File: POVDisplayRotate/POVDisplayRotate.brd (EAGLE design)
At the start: 54 x 82 mm, 38 parts, among them U1 CY8CKIT-142, U2 STP08DP05, U3 STP08DP05, U4 STP08DP05, U5 MPQ4420Q

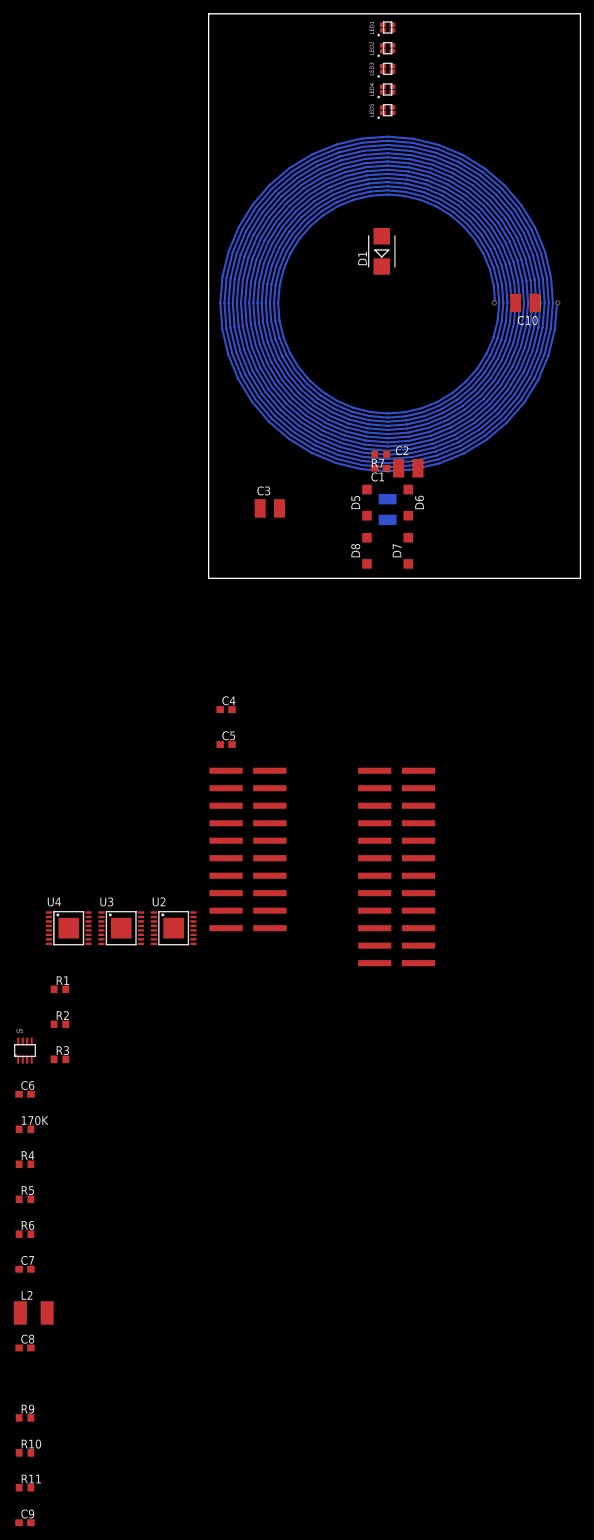
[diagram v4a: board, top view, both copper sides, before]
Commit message: Placed most of the components for the POVRotate. Working on PCB.
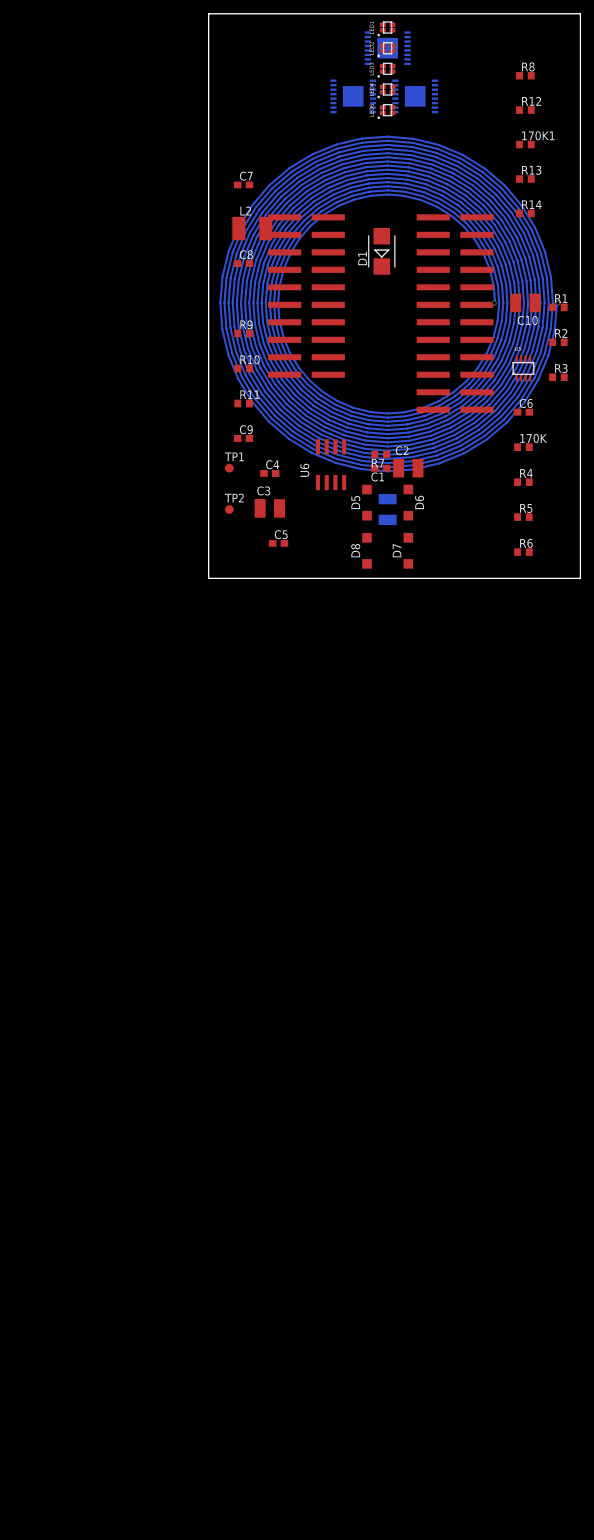
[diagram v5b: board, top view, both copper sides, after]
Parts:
- added 170K1: 120, resistor:R0603
- added R12: 820k, resistor:R0603
- added R13: 12k, resistor:R0603
- added R14: 3k, resistor:R0603
- added R8: 33k, resistor:R0603
- added TP1, TP2: TPB1,27, testpad:B1,27
- added U6: M95M01, NicksParts:SO-08
- moved C8 160.6 mm to (5.08, 45.7)
- moved L2 160.6 mm to (6.35, 50.8)
- moved R11 160.6 mm to (5.08, 25.4)
- moved R9 160.6 mm to (5.08, 35.6)
- moved C7 160.6 mm to (5.08, 57.1)
- moved C9 160.6 mm to (5.08, 20.3)
- moved R10 160.6 mm to (5.08, 30.5)
- moved U2 131.5 mm to (26.0, 77.0), flipped to the bottom, turned to 180 degrees
- moved U3 128.1 mm to (30.0, 70.0), flipped to the bottom
- moved U4 127.7 mm to (21.0, 70.0), flipped to the bottom
- moved 170K 122.7 mm to (45.7, 19.1)
- moved C6 122.7 mm to (45.7, 24.1)
- moved R1 122.7 mm to (50.8, 39.4)
- moved R2 122.7 mm to (50.8, 34.3)
- moved R3 122.7 mm to (50.8, 29.2)
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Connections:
- new net DAC_OUT: R13.2, R14.1, U1.2.1
- new net EE_CS: U1.0.2, U6.1
- new net EE_HOLD: U6.7
- new net EE_MISO: U1.0.1, U6.2
- new net EE_MOSI: U1.0.0, U6.5
- new net EE_SCLK: U1.0.3, U6.6
- new net EE_WP: U6.3
- new net GND: U6.4
- new net IN_PWR: R12.2, R8.1, U1.3.0
- new net N$13: TP1.TP, U5.1
- new net N$16: 170K1.1, C2.1, D5.C, D8.C
- new net N$3: U1.1.6
- net AGND: now also R14.2, R8.2
- net OPAMP1_NEG: now also U1.2.4, U1.2.7
- net OPAMP1_OUT: now also TP2.TP, U1.2.3
- net SCLK: now also U1.1.7
- net SDI: now also U1.0.4
- net V+: now also 170K1.2, R12.1; no longer C2.1, D5.C, D8.C
- net VCC: now also R13.1, U6.8

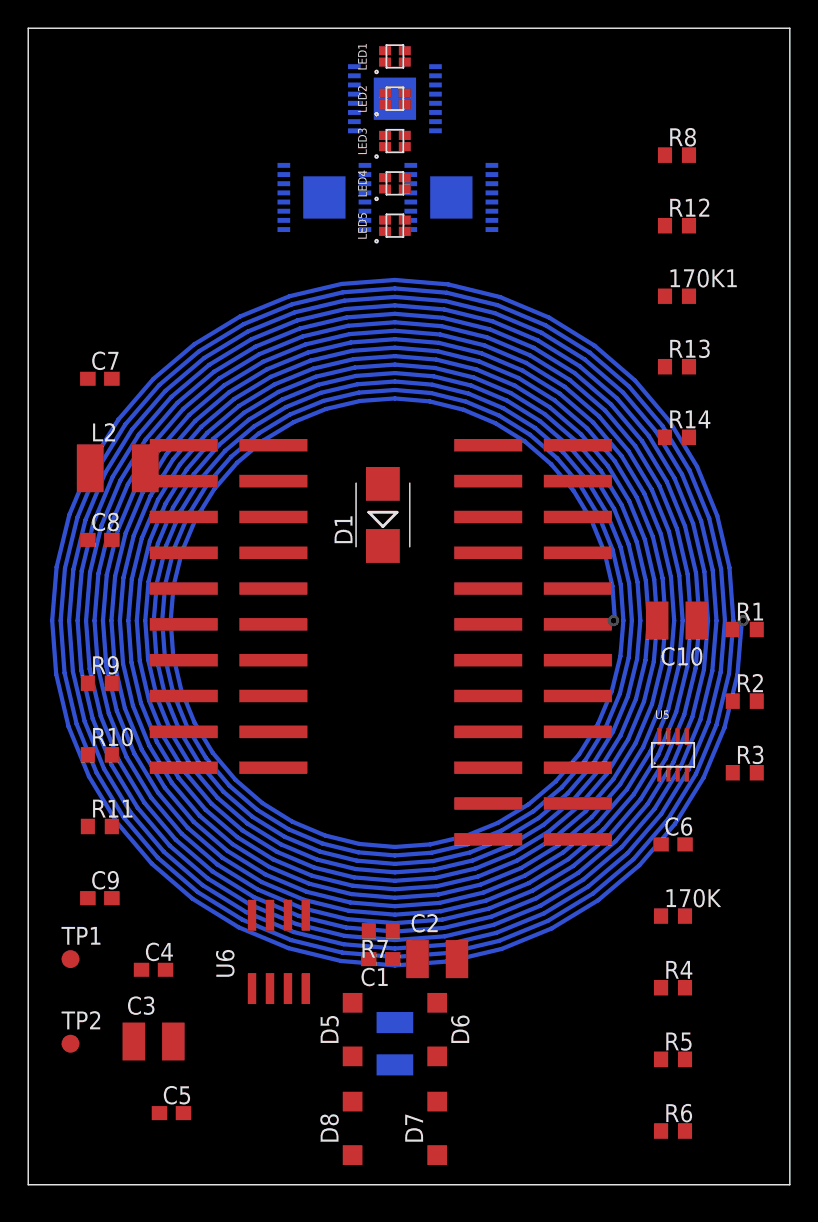
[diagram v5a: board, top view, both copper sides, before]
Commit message: Working on the routing of the POVRotate display.
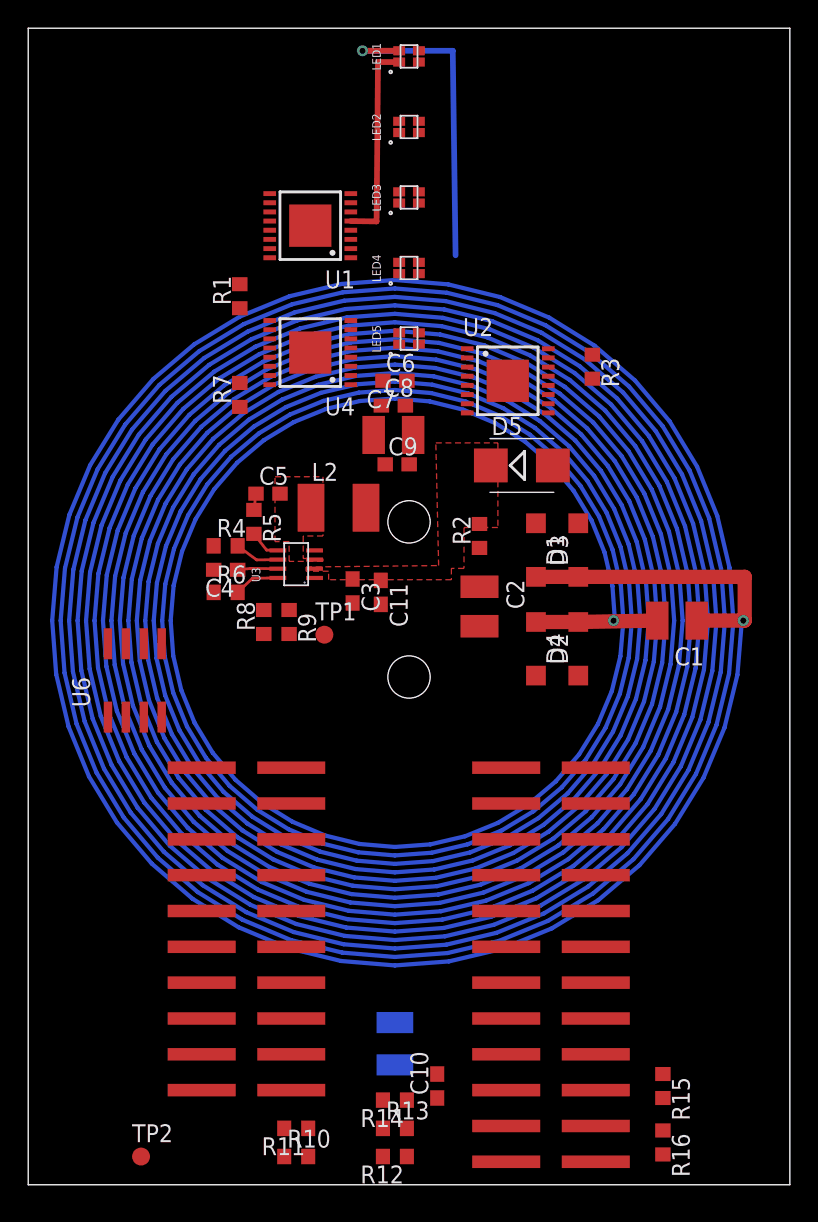
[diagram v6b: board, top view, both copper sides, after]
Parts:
- removed 170K, 170K1: 120, resistor:R0603
- removed D7, D8: (no value), diode:SOD123
- added C11: 0.1u, resistor:C0603
- added D3, D4: (no value), diode:SOD123
- added R15: 12k, resistor:R0603
- added R16: 3k, resistor:R0603
- C1: value 22u -> 100n; device resistor:C0603 -> resistor:C1210
- C10: value 100n -> 5p; device resistor:C1210 -> resistor:C0603
- C3: value 100u -> 22u; device resistor:C1210 -> resistor:C0603
- C4: value 10u -> 0.1u
- C5: value 1u -> 100n
- C6: value 0.1u -> 47u
- C7: value 100n -> 100u; device resistor:C0603 -> resistor:C1210
- C8: value 47u -> 10u
- C9: value 5p -> 1u
- D1: device diode:SMB -> diode:SOD123
- D2: value OP980 -> (none); device NicksParts:PLCC-2 -> diode:SOD123
- D5: device diode:SOD123 -> diode:SMB
- D6: value (none) -> OP980; device diode:SOD123 -> NicksParts:PLCC-2
- R13: value 12k -> 33k
- R14: value 3k -> 100k
- R2: value 386 -> 120
- R4: value 41.2k -> 120
- R5: value 12k -> 20
- R6: value 20 -> 51k
- R7: value 51k -> 386
- R8: value 33k -> 12k
- R9: value 100k -> 41.2k
- U1: value CY8CKIT-142 -> STP08DP05; device NicksParts:CY8CKIT-142 -> NicksParts:SSOP16_EPAD
- U3: value STP08DP05 -> MPQ4420Q; device NicksParts:SSOP16_EPAD -> NicksParts:SOT-23-8
- U5: value MPQ4420Q -> CY8CKIT-142; device NicksParts:SOT-23-8 -> NicksParts:CY8CKIT-142
- moved R12 69.0 mm to (26.0, 2.00), turned to 180 degrees
- moved R13 57.6 mm to (26.0, 4.00)
- moved R14 51.1 mm to (26.0, 6.00), turned to 180 degrees
- moved R6 49.6 mm to (14.0, 42.0)
- moved R5 48.3 mm to (16.0, 47.0), turned to 270 degrees
- moved R4 44.6 mm to (14.0, 45.3)
- moved C5 44.4 mm to (17.0, 49.0)
- moved R8 44.2 mm to (16.7, 39.9), turned to 90 degrees
- moved R1 42.9 mm to (15.0, 63.0), turned to 90 degrees
- moved D5 41.8 mm to (35.0, 51.0), turned to 0 degrees
- moved R7 39.3 mm to (15.0, 56.0), turned to 90 degrees
- moved C6 38.3 mm to (26.0, 57.0)
- moved C9 37.3 mm to (26.2, 51.1)
- moved C10 37.1 mm to (29.0, 7.00), turned to 90 degrees
- moved C3 34.9 mm to (23.0, 42.1), turned to 270 degrees
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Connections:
- removed net N$9: C7.2, L2.1, U5.3
- new net SWOUT: C5.2, L2.1, U3.3
- net AGND: now also C11.2, C7.2, C9.2, D2.A, D5.A, D6.P$1, R13.2, R16.2, R7.2, U1.1, U3.4, U5.GND, U5.GND1, U5.GND2; no longer C1.2, C5.2, D2.P$1, D6.A, D7.A, R14.2, R2.2, R5.2, U1.GND1, U1.GND2, U3.1, U3.GND, U5.4
- net DAC_OUT: now also R15.2, R16.1, U5.2.1; no longer R13.2, R14.1, U1.2.1
- net EE_CS: now also U5.0.2; no longer U1.0.2
- net EE_MISO: now also U5.0.1; no longer U1.0.1
- net EE_MOSI: now also U5.0.0; no longer U1.0.0
- net EE_SCLK: now also U5.0.3; no longer U1.0.3
- net GLED1: now also U2.5; no longer U3.5
- net GLED2: now also U2.6; no longer U3.6
- net GLED3: now also U2.7; no longer U3.7
- net GLED4: now also U2.8; no longer U3.8
- net GLED5: now also U2.9; no longer U3.9
- net IN_PWR: now also R13.1, U5.3.0; no longer R8.1, U1.3.0
- net LE1: now also U1.4; no longer U2.4
- net LE2: now also U2.4; no longer U3.4
- net N$1: now also C4.1, U3.7; no longer C6.1, U5.7
- net N$10: now also R3.1, U2.15; no longer R2.1, U3.15
- net N$11: now also U2.14; no longer U3.14
- net N$12: now also R7.1; no longer R3.1
- net N$13: now also U3.1; no longer U5.1
- net N$16: now also D3.C, D4.C, R2.1; no longer 170K1.1, D5.C, D8.C
- net N$18: now also U1.14, U2.2; no longer U2.14, U3.2
- net N$2: now also R4.2, U3.6; no longer 170K.2, U5.6
- net N$3: now also U5.1.6; no longer U1.1.6
- net N$4: now also R6.2, U3.8; no longer R7.2, U5.8
- net N$5: now also R6.1, R8.1, R9.2; no longer R4.2, R5.1, R7.1
- net N$6: now also U1.15; no longer U2.15
- net N$7: now also R5.2, U3.5; no longer R6.2, U5.5
- net N$8: now also C5.1, R5.1; no longer C7.1, R6.1
- net NEG_COIL: now also C1.2, D2.C, D4.A; no longer C10.2, D7.C, D8.A
- net OE1: now also U1.13; no longer U2.13
- net OE2: now also U2.13; no longer U3.13
- net OPAMP1_NEG: now also C10.2, D6.P$2, R14.2, U5.2.4, U5.2.7; no longer C9.2, D2.P$2, R9.2, U1.2.4, U1.2.7
- net OPAMP1_OUT: now also C10.1, R14.1, U5.2.3; no longer C9.1, R9.1, U1.2.3
- net POS_COIL: now also C1.1, D1.C, D3.A; no longer C10.1, D5.A, D6.C
- net RLED1: now also U1.5; no longer U2.5
- net RLED2: now also U1.6; no longer U2.6
- net RLED3: now also U1.7; no longer U2.7
- net RLED4: now also U1.8; no longer U2.8
- net RLED5: now also U1.9; no longer U2.9
- net SCLK: now also U1.3, U5.1.7; no longer U1.1.7, U3.3
- net SDI: now also U1.2, U5.0.4; no longer U1.0.4, U2.2
- net V+: now also C11.1, C3.1, D5.C, R2.2, R4.1, U3.2; no longer 170K.1, 170K1.2, C1.1, D1.C, U5.2
- net VCC: now also C6.1, C7.1, C9.1, R15.1, R9.1, U1.16, U5.VDDA, U5.VDDD, U5.VDDR; no longer C3.1, C4.1, C5.1, R13.1, R4.1, U1.VDDA, U1.VDDD, U1.VDDR, U3.16
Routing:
- net GLED1: track 0.00 -> 23.5 mm, vias 0 -> 1
- net POS_COIL: track 0.00 -> 21.3 mm
- net RLED1: track 0.00 -> 14.6 mm
- net NEG_COIL: track 0.00 -> 8.60 mm
- net N$4: track 0.00 -> 3.25 mm
- net N$2: track 0.00 -> 3.18 mm
- net N$1: track 0.00 -> 2.86 mm
- net N$7: track 0.00 -> 2.26 mm
- net N$8: track 0.00 -> 1.16 mm
- added copper zone on layer 1, net SWOUT
- added copper zone on layer 1, net V+

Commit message: More routing.
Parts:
- removed R7: 386, resistor:R0603
- removed U4: STP08DP05, NicksParts:SSOP16_EPAD
- moved R1 8.25 mm to (13.0, 71.0), turned to 0 degrees
- moved R3 8.06 mm to (36.0, 65.0), turned to 180 degrees
- moved U6 6.00 mm to (13.6, 35.8)
- moved U2 3.61 mm to (36.0, 60.0)
- moved U1 1.00 mm to (21.0, 68.0), turned to 0 degrees
- moved C9 0.50 mm to (25.9, 50.7)
- moved C6 0.41 mm to (25.9, 56.6)
- moved C7 0.20 mm to (25.9, 53.0)
- moved C8 0.10 mm to (25.9, 55.1)
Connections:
- removed net LE3: U4.4
- removed net N$11: U2.14, U4.2
- removed net N$12: R7.1, U4.15
- removed net OE3: U4.13
- net AGND: no longer R7.2, U4.1, U4.GND
- net BLED1: now also U1.7; no longer U4.5
- net BLED2: now also U1.10; no longer U4.6
- net BLED3: now also U2.5; no longer U4.7
- net BLED4: now also U2.8; no longer U4.8
- net BLED5: now also U2.11; no longer U4.9
- net GLED1: now also U1.6; no longer U2.5
- net GLED2: now also U1.9; no longer U2.6
- net GLED3: now also U1.12; no longer U2.7
- net GLED4: now also U2.7; no longer U2.8
- net GLED5: now also U2.10; no longer U2.9
- net RLED2: now also U1.8; no longer U1.6
- net RLED3: now also U1.11; no longer U1.7
- net RLED4: now also U2.6; no longer U1.8
- net RLED5: now also U2.9; no longer U1.9
- net SCLK: no longer U4.3
- net VCC: no longer U4.16
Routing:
- net VCC: track 0.00 -> 95.9 mm, vias 0 -> 7
- net SDI: track 0.00 -> 52.8 mm
- net BLED5: track 0.00 -> 35.4 mm
- net N$16: track 0.00 -> 32.8 mm
- net GLED5: track 0.00 -> 26.0 mm
- net BLED1: track 0.00 -> 25.1 mm, vias 0 -> 2
- net BLED4: track 0.00 -> 19.9 mm
- net RLED5: track 0.00 -> 17.9 mm
- net GLED2: track 0.00 -> 16.5 mm, vias 0 -> 2
- net BLED3: track 0.00 -> 16.2 mm
- net RLED2: track 0.00 -> 15.9 mm, vias 0 -> 2
- net GLED4: track 0.00 -> 15.7 mm
- net BLED2: track 0.00 -> 15.4 mm, vias 0 -> 2
- net V+: track 0.00 -> 14.9 mm, vias 0 -> 2
- net RLED4: track 0.00 -> 12.4 mm
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- added copper zone on layer 1, net N$9
